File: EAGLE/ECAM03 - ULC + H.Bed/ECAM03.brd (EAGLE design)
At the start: 160 x 60 mm, 41 parts, among them J1 MODULAR TOOL, J2 FAN1, J3 FAN2, J4 FAN3, J5 S4B-PH-SM4, J6 SSR, J7 RINGLIGHT, Q2 16MHz, U1 SP3485, U2 ATMEGA238, U3 MCP4725, U4 MAX31855, U5 NTR4003NT3G, U6 NOR(74LVC), U8 AP3032

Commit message: Final(??) Versions of FPD boards.
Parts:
- added C6: 0.1uF, TinWhiskers:C0603
- added J8: FTDI, TinWhiskers:CON-HDR-6POS-MALE
- added J9: SPI, TinWhiskers:CON-HDR-2X3P
- added R14: 10K, TinWhiskers:R0603
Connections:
- new net N$16: C6.1, J8.6
- net +5V: now also J8.3, J9.2, R14.2
- net DI: now also J8.5
- net GND: now also J8.1, J8.2, J9.6
- net MISO: now also J9.1
- net MOSI: now also J9.4
- net RESET: now also C6.2, J9.5, R14.1
- net RO: now also J8.4
- net SCK: now also J9.3
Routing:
- net MOSI: track 0.00 -> 192.6 mm, vias 0 -> 4
- net MISO: track 25.2 -> 201.9 mm, vias 2 -> 4
- net SCK: track 36.2 -> 196.9 mm, vias 2 -> 4
- net RESET: track 0.00 -> 126.3 mm, vias 0 -> 4
- net RO: track 10.7 -> 124.7 mm, vias 0 -> 6
- net DI: track 16.1 -> 109.7 mm, vias 0 -> 3
- net GND: track 367.1 -> 399.4 mm, vias 15 -> 16
- net +5V: track 300.6 -> 329.6 mm, vias 9 -> 10
- net N$16: track 0.00 -> 5.76 mm

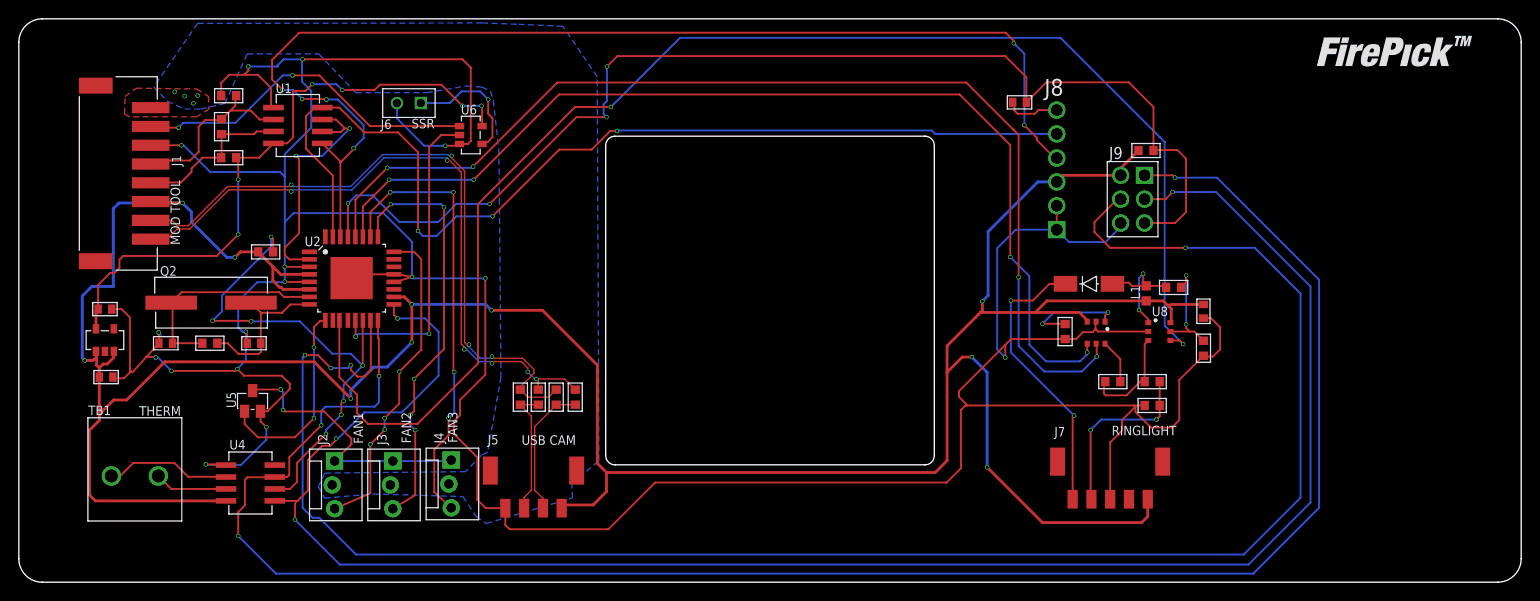
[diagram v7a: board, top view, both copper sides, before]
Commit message: Re-jiggered switching power for LED controller, rerouted and whatnot.  Added trace for WS2812B.  Swapped DAC wire (A0 was going to the LED driver instead of analog out).  Generated GERBERs for Rev--.
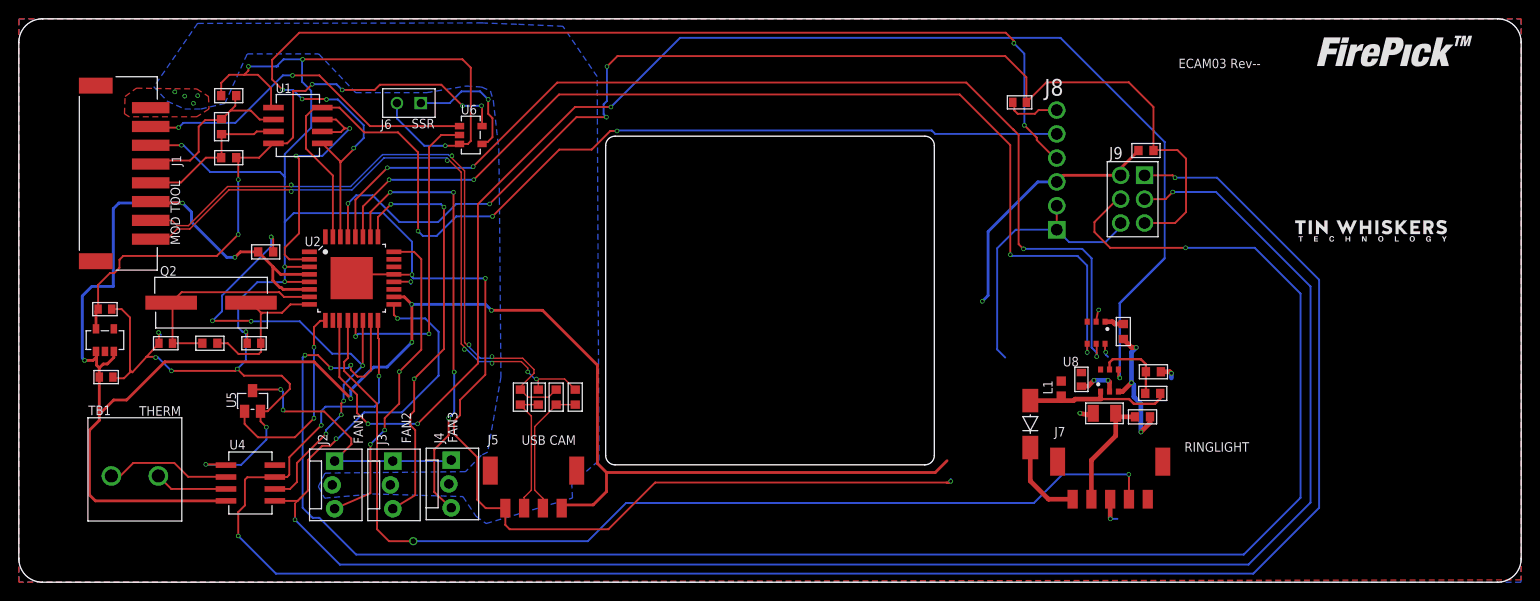
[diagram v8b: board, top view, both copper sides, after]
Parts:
- removed R5: 5K, TinWhiskers:R0603
- added U$1: TIN-WHISKERSTSTOP, !tin-whiskers-logo:TIN-WHISKERS-TSTOP
- R7: device TinWhiskers:R0603 -> TinWhiskers:R1206
- moved D1 16.2 mm to (107.7, 16.8), turned to 270 degrees
- moved C12 14.9 mm to (113.2, 21.6)
- moved L1 13.6 mm to (111.0, 20.6), turned to 270 degrees
- moved R15 11.5 mm to (120.8, 20.1), turned to 0 degrees
- moved U8 7.44 mm to (116.2, 21.5), turned to 180 degrees
- moved R16 5.89 mm to (120.8, 22.4), turned to 180 degrees
- moved R12 5.45 mm to (117.6, 26.7), turned to 90 degrees
- moved R7 5.15 mm to (115.6, 18.0)
- moved R6 3.89 mm to (119.7, 17.6), turned to 180 degrees
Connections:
- net N$1 renamed LED_+
- net N$2 renamed LED_SW
- net N$4 renamed LED_FB
- net N$6 renamed LED_-
- net OV renamed LED_OV
- removed net A0: R12.2, U3.6
- new net WS2812B: J7.4, U2.12
- net GND: now also U3.6; no longer R5.1
- net N$5: now also R12.2; no longer R5.2
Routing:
- net WS2812B: track 0.00 -> 110.0 mm, vias 0 -> 2
- net +5V: track 329.6 -> 241.3 mm, vias 10 -> 8
- net GND: track 399.4 -> 327.0 mm, vias 16 -> 24
- net LED_+: track 30.6 -> 8.87 mm, vias 2 -> 0
- net N$5: track 11.0 -> 2.05 mm, vias 2 -> 0
- net LED_-: track 19.1 -> 12.4 mm, vias 2 -> 0
- net A0: track 4.71 -> 0.00 mm
- net LED_FB: track 10.9 -> 15.2 mm, vias 0 -> 3
- net CTRL: track 152.6 -> 156.8 mm, vias 2 -> 4
- net LED_OV: track 11.5 -> 8.13 mm, vias 2 -> 0
- net LED_SW: track 13.2 -> 16.2 mm, vias 2 -> 0
- net SCL: track 116.0 -> 114.2 mm
- net TACH2: vias 5 -> 3
- net TACH1: vias 4 -> 3
- added copper zone on layer 1, net +5V
- added copper zone on layer 16, net GND
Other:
- board text added: "ECAM03 Rev--"
